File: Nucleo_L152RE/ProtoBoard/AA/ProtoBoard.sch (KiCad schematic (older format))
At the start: 127 parts, among them CON1 USB-MICRO-B, J1 EXT1, J2 EXT2, J3 EXTPower, P1 Power, P10 OW2_A, P11 CONN_01X06, P12 I2C1_B, P13 I2C2_B, P14 SW_1_6, P15 WS_1_2, P16 WS_3_4, P17 MS2, P18 OW1_B, P19 OW2_B, P2 VinPower, P20 I2C1_C, P21 I2C2_C, P22 MS3, P23 OW3_A, P24 OW4_A, P25 MS4, P26 OW3_B, P27 OW4_B, P28 RGB1, P29 Ant, P3 USART2, P4 SWD Header, P5 USART1, P6 MS1, P7 I2C1_A, P8 I2C2_A, P9 OW1_A, Q1 SI2323DS, SW1 MomentarySwitch, U2 Nucleo-L152RE-CN7, U3 Nucleo-L152RE-CN10, U5 MT3329_GPS, U6 S25FL127S, U7 RFM69HW

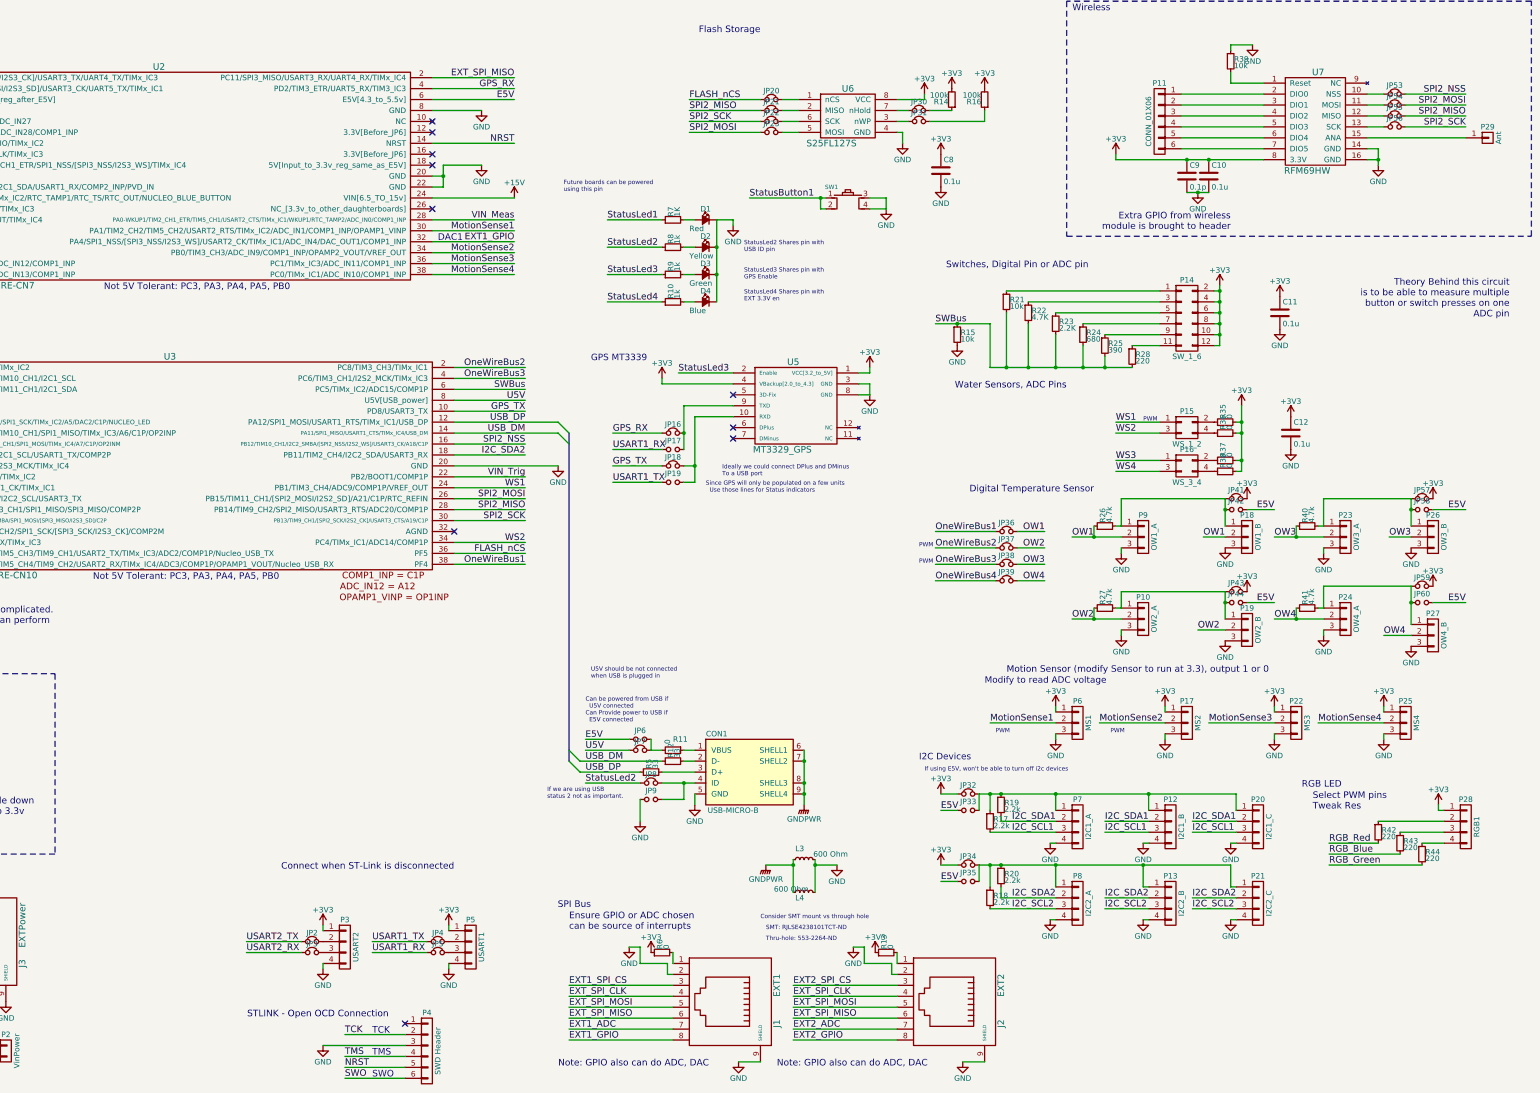
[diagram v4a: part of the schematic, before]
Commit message: all remaining components fit on one board.
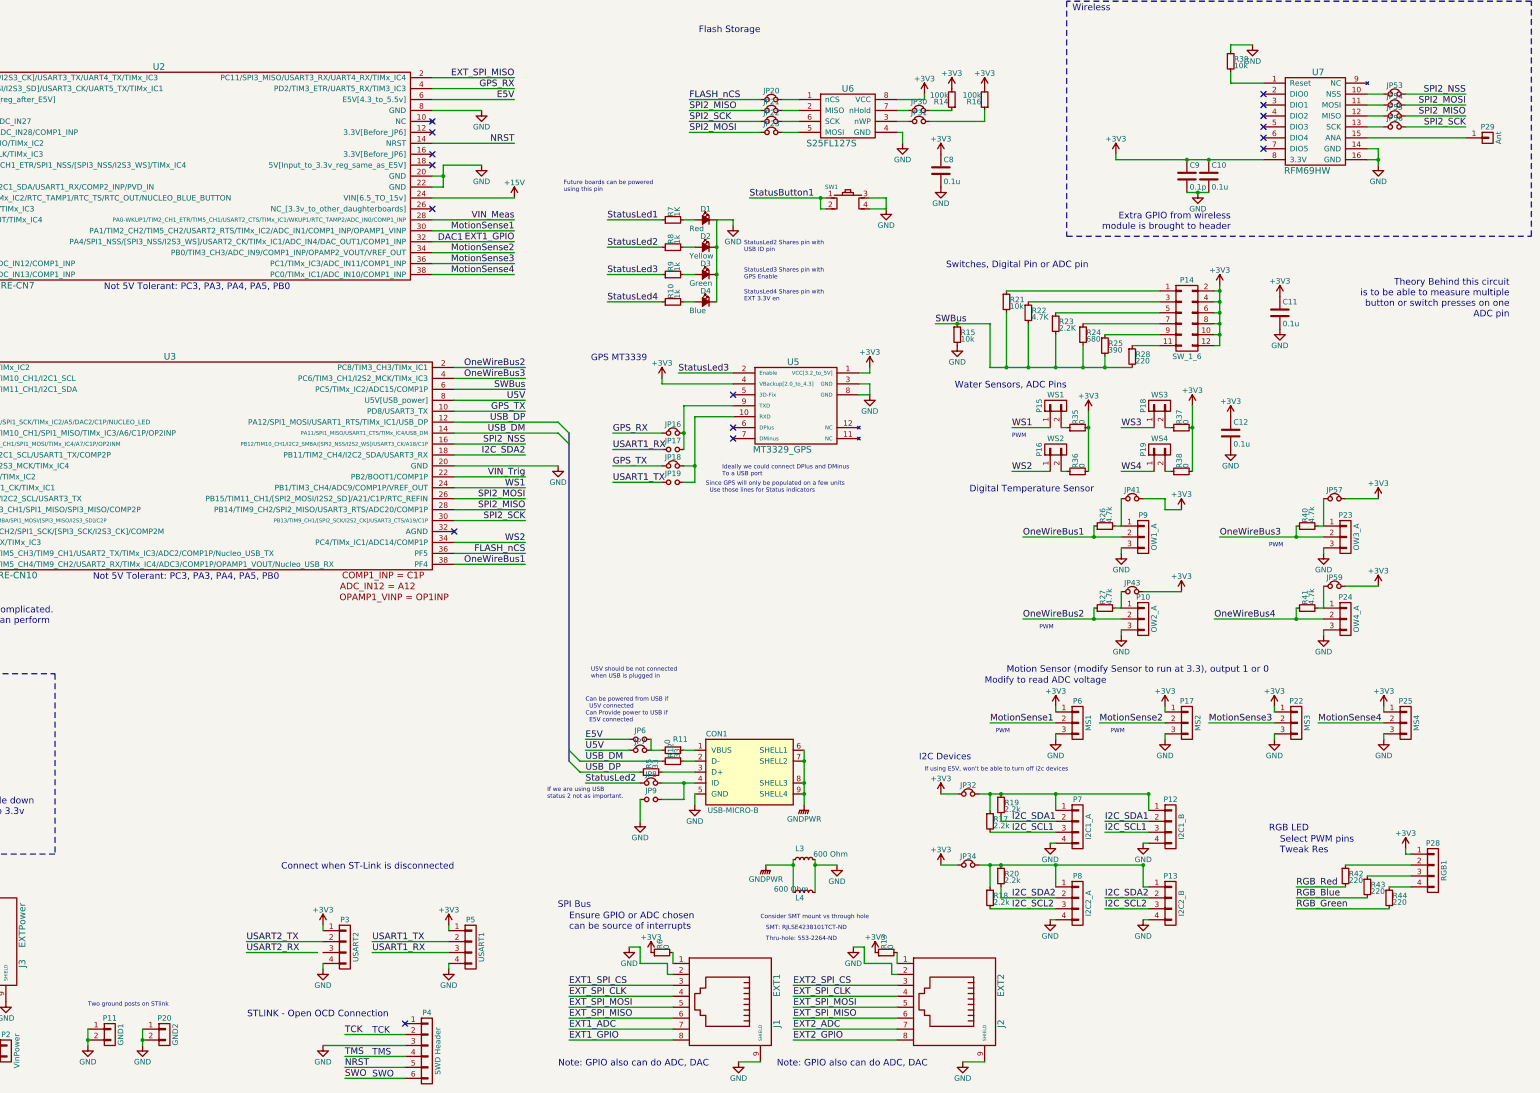
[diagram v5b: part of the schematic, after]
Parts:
- removed JP2, JP3, JP36, JP37, JP38, JP39, JP4, JP5: Jumper_NC_Small, nucleo:SB_NC, symbol Jumper_NC_Small
- removed JP33, JP35, JP42, JP44, JP58, JP60: Jumper_NO_Small, nucleo:SB_NO, symbol Jumper_NO_Small
- removed P11: CONN_01X06, Pin_Headers:Pin_Header_Straight_1x06, symbol CONN_01X06
- removed P15: WS_1_2, Pin_Headers:Pin_Header_Straight_2x02, symbol CONN_02X02
- removed P16: WS_3_4, Pin_Headers:Pin_Header_Straight_2x02, symbol CONN_02X02
- removed P18: OW1_B, Pin_Headers:Pin_Header_Straight_1x03, symbol CONN_01X03
- removed P19: OW2_B, Pin_Headers:Pin_Header_Straight_1x03, symbol CONN_01X03
- removed P20: I2C1_C, Pin_Headers:Pin_Header_Straight_1x04, symbol CONN_01X04
- removed P21: I2C2_C, Pin_Headers:Pin_Header_Straight_1x04, symbol CONN_01X04
- removed P26: OW3_B, Pin_Headers:Pin_Header_Straight_1x03, symbol CONN_01X03
- removed P27: OW4_B, Pin_Headers:Pin_Header_Straight_1x03, symbol CONN_01X03
- added P11: GND1, Pin_Headers:Pin_Header_Straight_1x02, symbol CONN_01X02
- added P15: WS1, Pin_Headers:Pin_Header_Straight_1x02, symbol CONN_01X02
- added P16: WS2, Pin_Headers:Pin_Header_Straight_1x02, symbol CONN_01X02
- added P18: WS3, Pin_Headers:Pin_Header_Straight_1x02, symbol CONN_01X02
- added P19: WS4, Pin_Headers:Pin_Header_Straight_1x02, symbol CONN_01X02
- added P20: GND2, Pin_Headers:Pin_Header_Straight_1x02, symbol CONN_01X02
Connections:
- net OW1 is gone; now on net OneWireBus1: P9.2 (P2), R26.1
- net OW2 is gone; now on net OneWireBus2: P10.2 (P2), R27.1
- net OW3 is gone; now on net OneWireBus3: P23.2 (P2), R40.1
- net OW4 is gone; now on net OneWireBus4: P24.2 (P2), R41.1
- net GND: now also P11.1 (P1), P11.2 (P2), P20.1 (P1), P20.2 (P2)
- net USART1_RX: now also P5.3 (P3)
- net USART1_TX: now also P5.2 (P2)
- net USART2_TX: now also P3.2 (P2)
- net WS1: now also P15.1 (P1)
- net WS2: now also P16.1 (P1)
- net WS3: now also P18.1 (P1)
- net WS4: now also P19.1 (P1)
- net at R35.1: now also P15.2 (P2)
- net at R36.1: now also P16.2 (P2)
- net at R38.1: now also P19.2 (P2)
- net at R37.1: now also P18.2 (P2)
- no-connect marks 13 -> 19
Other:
- note added: "Two ground posts on STlink"
- moved on the sheet: C12, JP41, JP43, JP57, JP59, P28, R35, R36, R37, R38, R42, R43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

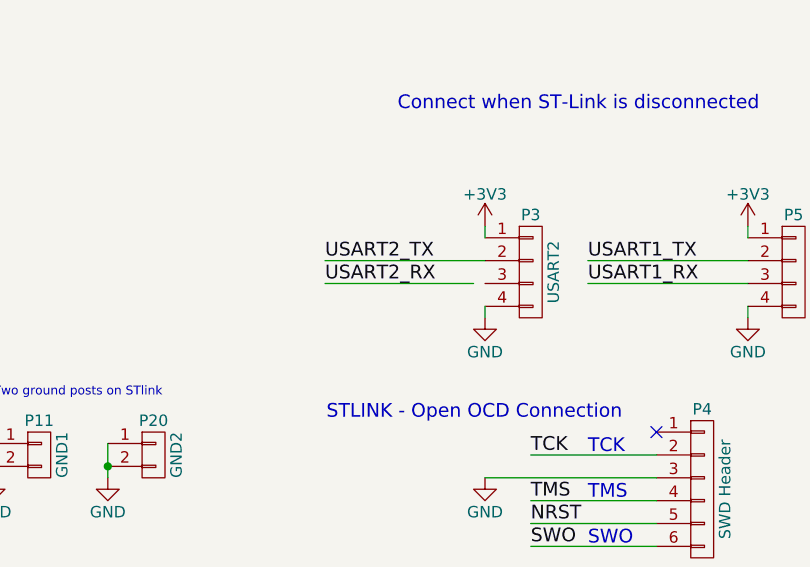
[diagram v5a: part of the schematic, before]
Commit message: performing more routing of the board.  This board is quickly becoming complicated with all of the headers to navigate around.
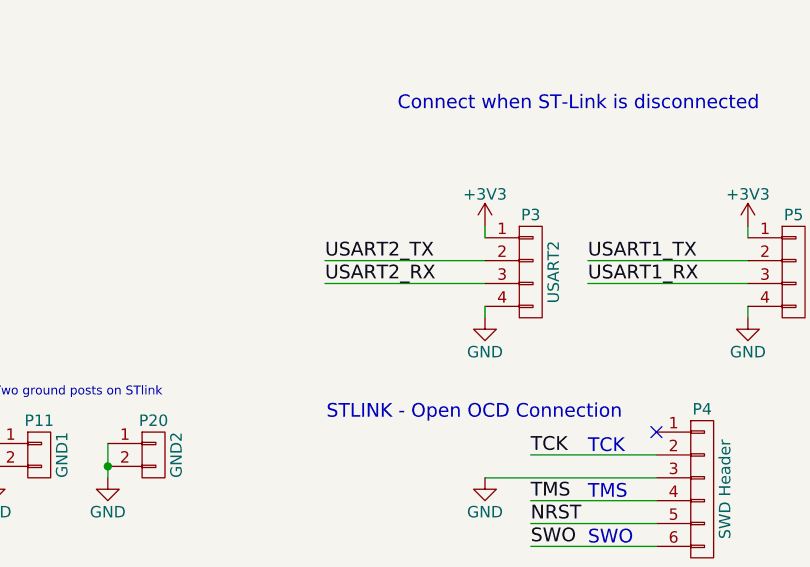
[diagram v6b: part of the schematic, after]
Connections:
- net USART2_RX: now also P3.3 (P3)
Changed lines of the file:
@@
 	4750 9100 5450 9100
 Wire Wire Line
-	4750 9200 5400 9200
+	4750 9200 5450 9200
 Wire Wire Line
 	6600 9350 6600 9300

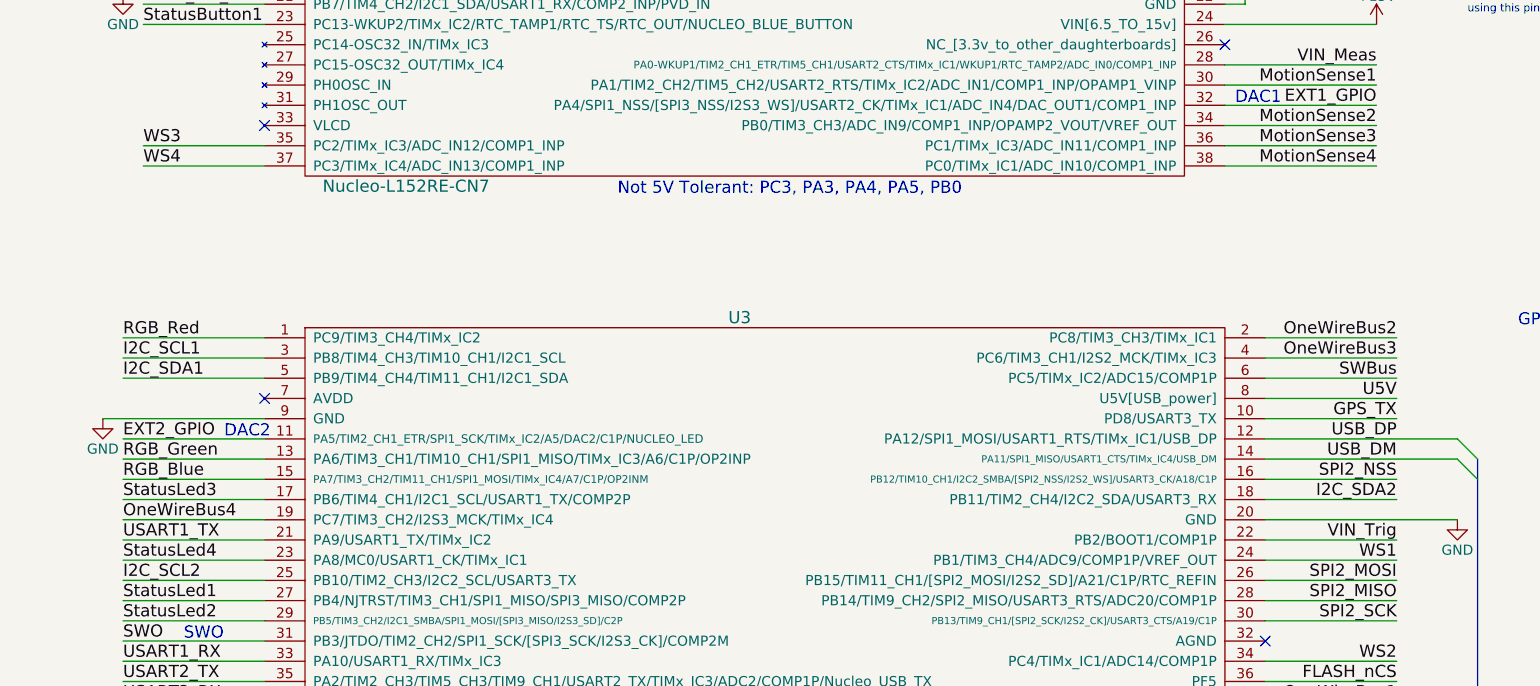
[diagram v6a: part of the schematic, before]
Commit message: All signals routed, now the only remaining thing is ground signals and/or ground planes.
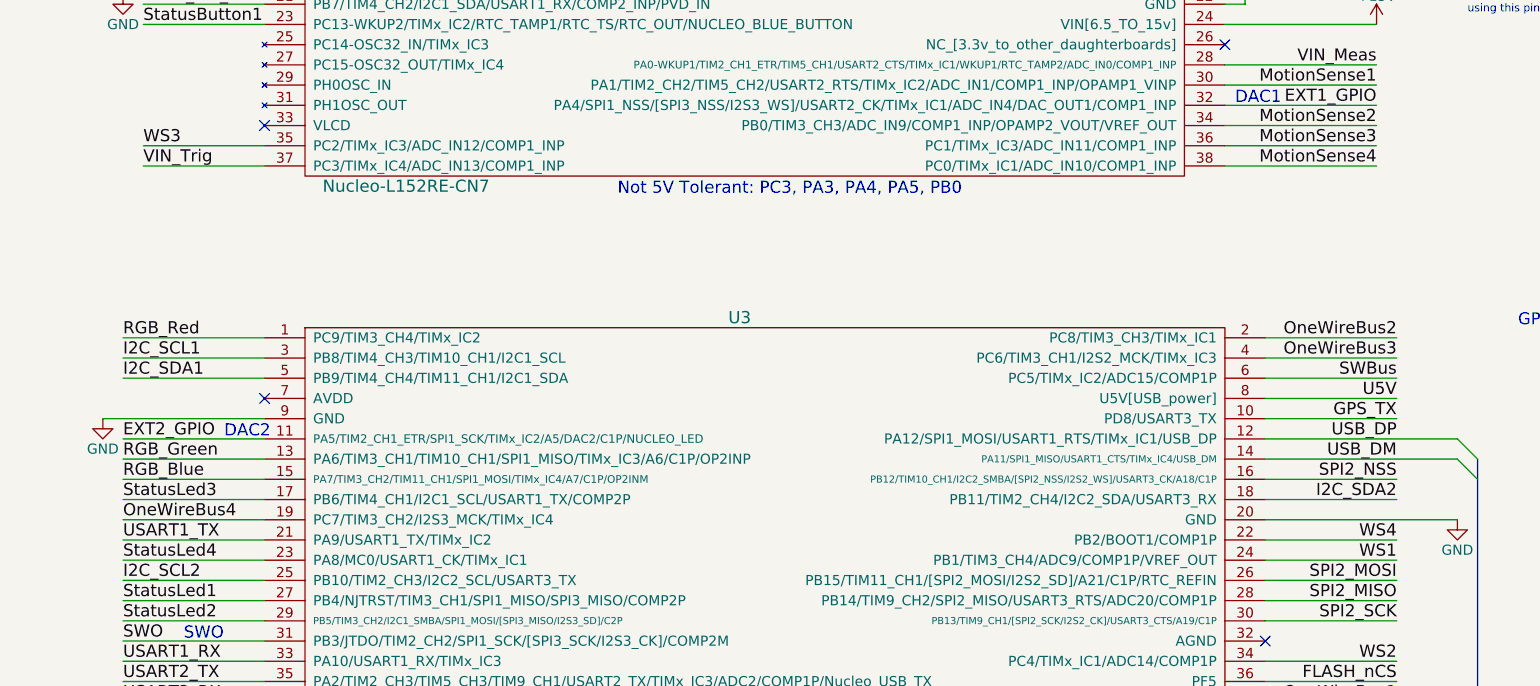
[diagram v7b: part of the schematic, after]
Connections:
- net VIN_Trig: now also U2.37 (PC3/TIMx_IC4/ADC_IN13/COMP1_INP); no longer U3.22 (PB2/BOOT1/COMP1P)
- net WS4: now also U3.22 (PB2/BOOT1/COMP1P); no longer U2.37 (PC3/TIMx_IC4/ADC_IN13/COMP1_INP)
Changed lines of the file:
@@
 Text Label 1100 2900 0    60   ~ 0
 WS3
-Text Label 1100 3000 0    60   ~ 0
+Text Label 7300 4850 2    60   ~ 0
 WS4
 Text Label 7200 1400 2    60   ~ 0
@@
 Text Label 9350 2300 0    60   ~ 0
 StatusButton1
-Text Label 7300 4850 2    60   ~ 0
+Text Label 1100 3000 0    60   ~ 0
 VIN_Trig
 Text Label 7300 4150 2    60   ~ 0

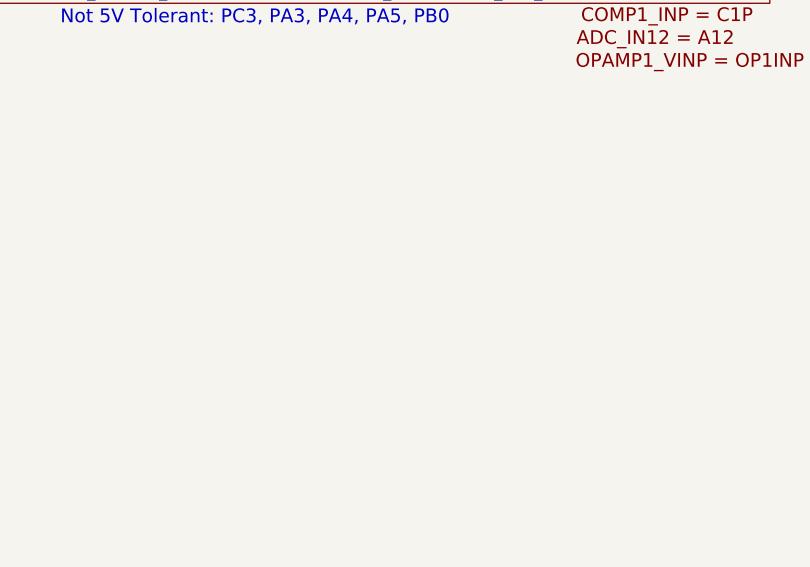
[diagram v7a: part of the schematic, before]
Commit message: About to modify Solder Bridges to be a smaller 0402 package rather than the custom one which generates DRC errors.
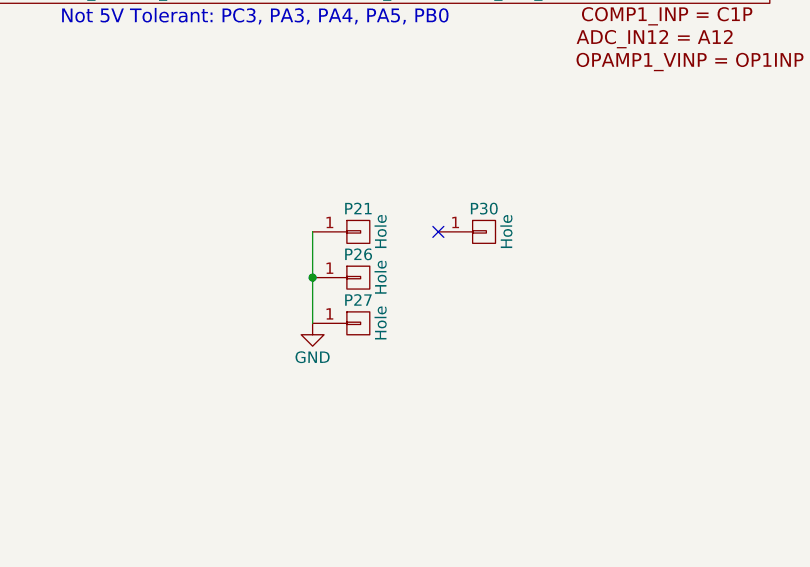
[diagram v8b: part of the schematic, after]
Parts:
- added P21, P26, P27: Hole, nucleo:plat_hole_4_20, symbol CONN_01X01
- added P30: Hole, Mounting_Holes:MountingHole_3mm, symbol CONN_01X01
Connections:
- net GND: now also P21.1 (P1), P26.1 (P1), P27.1 (P1)
- no-connect marks 19 -> 20
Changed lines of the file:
@@
 Text Notes 3300 9700 0    39   ~ 0
 Two ground posts on STlink
+$Comp
+L CONN_01X01 P21
+U 1 1 552D67CC
+P 4650 6700
+F 0 "P21" H 4650 6800 50  0000 C CNN
+F 1 "Hole" V 4750 6700 50  0000 C CNN
+F 2 "nucleo:plat_hole_4_20" H 4650 6700 60  0001 C CNN
+F 3 "" H 4650 6700 60  0000 C CNN
+	1    4650 6700
+	1    0    0    -1
+$EndComp
+$Comp
+L GND #PWR079
+U 1 1 552D72B3
+P 4450 7100
+F 0 "#PWR079" H 4450 6850 50  0001 C CNN
+F 1 "GND" H 4450 6950 50  0000 C CNN
+F 2 "" H 4450 7100 60  0000 C CNN
+F 3 "" H 4450 7100 60  0000 C CNN
+	1    4450 7100
+	1    0    0    -1
+$EndComp
+Connection ~ 4450 6900
+$Comp
+L CONN_01X01 P26
+U 1 1 552D814E
+P 4650 6900
+F 0 "P26" H 4650 7000 50  0000 C CNN
+F 1 "Hole" V 4750 6900 50  0000 C CNN
+F 2 "nucleo:plat_hole_4_20" H 4650 6900 60  0001 C CNN
+F 3 "" H 4650 6900 60  0000 C CNN
+	1    4650 6900
+	1    0    0    -1
+$EndComp
+$Comp
+L CONN_01X01 P27
+U 1 1 552D8244
+P 4650 7100
+F 0 "P27" H 4650 7200 50  0000 C CNN
+F 1 "Hole" V 4750 7100 50  0000 C CNN
+F 2 "nucleo:plat_hole_4_20" H 4650 7100 60  0001 C CNN
+F 3 "" H 4650 7100 60  0000 C CNN
+	1    4650 7100
+	1    0    0    -1
+$EndComp
+$Comp
+L CONN_01X01 P30
+U 1 1 552D833C
+P 5200 6700
+F 0 "P30" H 5200 6800 50  0000 C CNN
+F 1 "Hole" V 5300 6700 50  0000 C CNN
+F 2 "Mounting_Holes:MountingHole_3mm" H 5200 6700 60  0001 C CNN
+F 3 "" H 5200 6700 60  0000 C CNN
+	1    5200 6700
+	1    0    0    -1
+$EndComp
+NoConn ~ 5000 6700
+Wire Wire Line
+	4450 6700 4450 7100
 $EndSCHEMATC
